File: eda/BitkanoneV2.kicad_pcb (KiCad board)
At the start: 2 copper layers, 140 parts, among them J202 5VUSB, J211 JH23, J212 JL23, J231 Jumper, J232 Jumper, J233 Jumper, J234 Jumper, Q501 PH_NPN, Q502 PH_NPN, U201 BluePill_STM32F103C, U202 MCP2551-I-SN, U301 6DOF, X101 01x02M, X102 01x02M, X200 01x03M, X201 5VUSB, X231 Bus, X232 Bus, X233 Bus, X234 Bus, X401 MotorCon, X42 Conn_01x07_Male, X990 Conn_01x01, X991 Conn_01x01

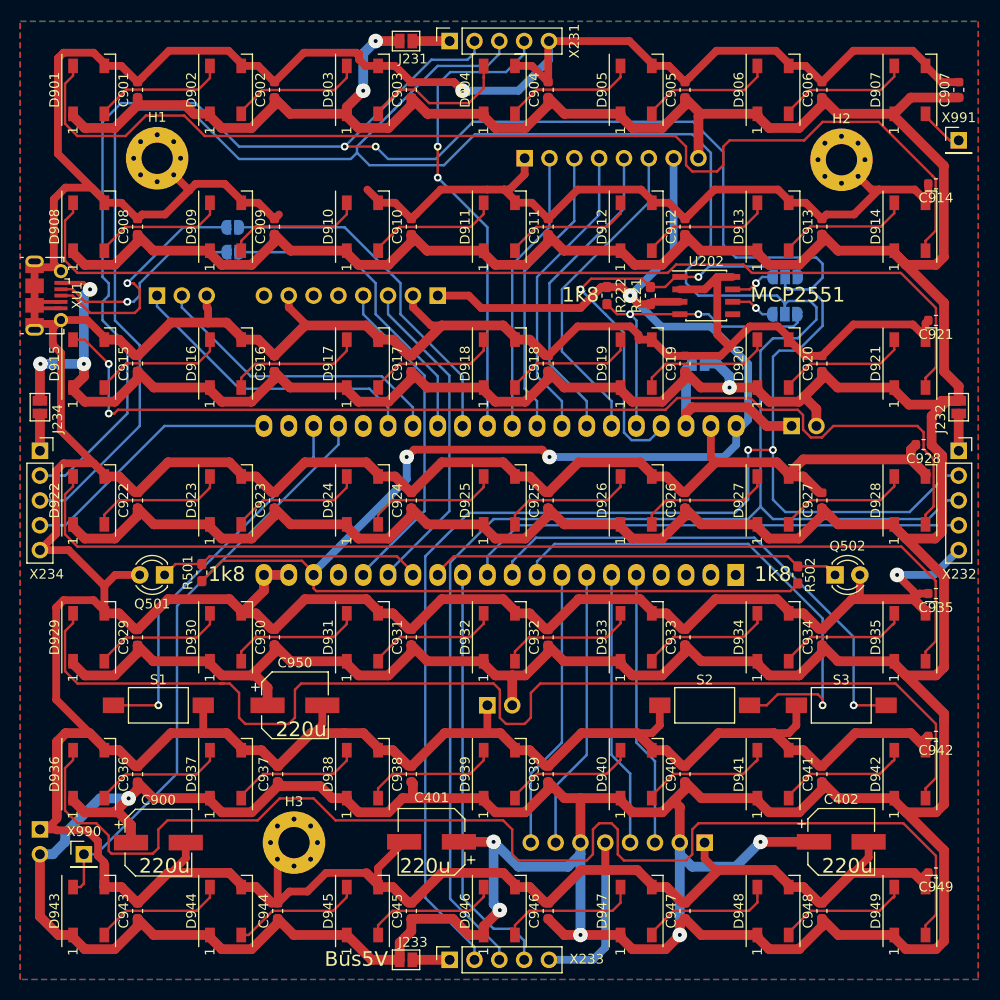
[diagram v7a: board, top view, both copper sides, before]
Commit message: bitkanoneV2 first PCB run ordered
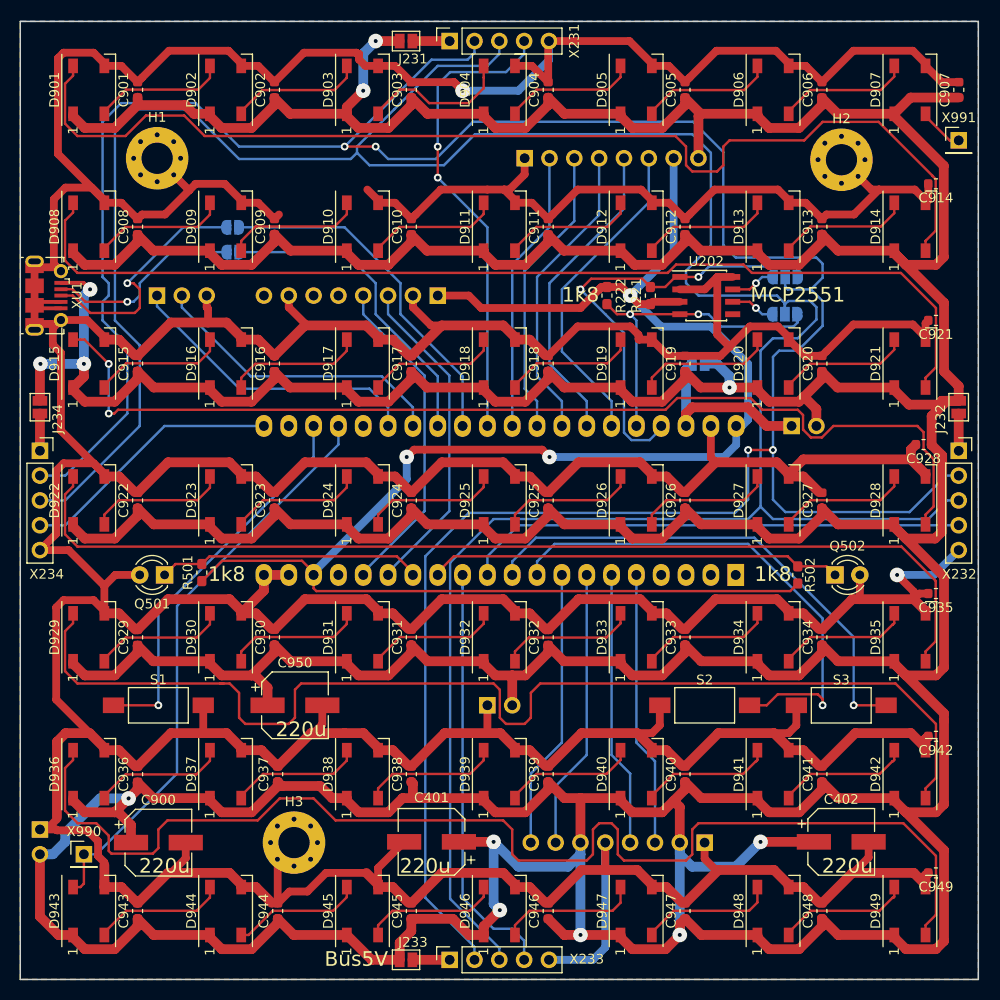
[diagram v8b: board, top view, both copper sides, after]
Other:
- board outline added: 98 x 98 mm
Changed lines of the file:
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@@
   (general
     (thickness 1.6)
-    (drawings 86)
+    (drawings 90)
     (tracks 1602)
     (zones 0)
@@
     (0 F.Cu signal)
     (31 B.Cu signal)
-    (32 B.Adhes user)
-    (33 F.Adhes user)
+    (32 B.Adhes user hide)
+    (33 F.Adhes user hide)
     (34 B.Paste user)
     (35 F.Paste user)
@@
     (38 B.Mask user)
     (39 F.Mask user)
-    (40 Dwgs.User user)
-    (41 Cmts.User user)
-    (42 Eco1.User user)
-    (43 Eco2.User user)
+    (40 Dwgs.User user hide)
+    (41 Cmts.User user hide)
+    (42 Eco1.User user hide)
+    (43 Eco2.User user hide)
     (44 Edge.Cuts user)
-    (45 Margin user)
+    (45 Margin user hide)
     (46 B.CrtYd user hide)
     (47 F.CrtYd user hide)
@@
     (solder_mask_min_width 0.25)
     (aux_axis_origin 0 0)
-    (grid_origin 47.4608 76.62)
+    (grid_origin 20 20)
     (visible_elements FFFFFFFF)
     (pcbplotparams
@@
       (usegerberadvancedattributes false)
       (creategerberjobfile false)
-      (excludeedgelayer true)
-      (linewidth 0.100000)
+      (excludeedgelayer false)
+      (linewidth 0.150000)
       (plotframeref false)
       (viasonmask false)
       (mode 1)
-      (useauxorigin false)
+      (useauxorigin true)
       (hpglpennumber 1)
       (hpglpenspeed 20)
@@
       (plotvalue true)
       (plotinvisibletext false)
-      (padsonsilk false)
+      (padsonsilk true)
       (subtractmaskfromsilk false)
       (outputformat 1)
       (mirror false)
-      (drillshape 1)
+      (drillshape 0)
       (scaleselection 1)
-      (outputdirectory ""))
+      (outputdirectory "plots/"))
   )
   (net 0 "")
@@
     )
   )
+  (gr_line (start 118 20) (end 20 20) (layer Edge.Cuts) (width 0.15))
+  (gr_line (start 118 118) (end 118 20) (layer Edge.Cuts) (width 0.15))
+  (gr_line (start 20 118) (end 118 118) (layer Edge.Cuts) (width 0.15))
+  (gr_line (start 20 20) (end 20 118) (layer Edge.Cuts) (width 0.15))
   (gr_text 98mm (at 103.3408 23.915) (layer B.SilkS)
     (effects (font (size 1.5 1.5) (thickness 0.3)) (justify mirror))
@@
   (segment (start 37.7558 29.45) (end 36.865802 28.560002) (width 1) (layer F.Cu) (net 7))
   (segment (start 24.1883 46.775) (end 24.1583 46.745) (width 0.25) (layer F.Cu) (net 7))
+  (via (at 27.1408 47.41) (size 1.5) (drill 0.4) (layers F.Cu B.Cu) (net 7))
+  (segment (start 24.1583 46.745) (end 26.4758 46.745) (width 0.4) (layer F.Cu) (net 7))
+  (segment (start 26.4758 46.745) (end 27.1408 47.41) (width 0.4) (layer F.Cu) (net 7))
+  (segment (start 26.5058 48.045) (end 27.1408 47.41) (width 1) (layer B.Cu) (net 7))
+  (segment (start 26.5058 55.03) (end 26.5058 48.045) (width 1) (layer B.Cu) (net 7))
   (segment (start 28.6 29.45) (end 28.6 29.2) (width 0.25) (layer F.Cu) (net 8))
   (segment (start 30.82499 26.97501) (end 38.21499 26.97501) (width 0.25) (layer F.Cu) (net 8))
@@
   (segment (start 71.54 115.99) (end 71.54 114.0342) (width 0.25) (layer B.Cu) (net 64))
   (segment (start 71.54 114.0342) (end 70.3208 112.815) (width 0.25) (layer B.Cu) (net 64))
+  (segment (start 22.01 71.54) (end 24.6008 71.54) (width 0.25) (layer B.Cu) (net 65))
+  (segment (start 34.7608 61.38) (end 44.9208 61.38) (width 0.25) (layer B.Cu) (net 65))
+  (segment (start 24.6008 71.54) (end 34.7608 61.38) (width 0.25) (layer B.Cu) (net 65))
   (segment (start 22.01 63.92) (end 22.01 60.11) (width 1) (layer F.Cu) (net 67))
   (segment (start 63.92 115.99) (end 60.11 115.99) (width 1) (layer F.Cu) (net 68))
@@
   (segment (start 53.1758 32.805) (end 42.3808 32.805) (width 0.25) (layer B.Cu) (net 80))
   (segment (start 30.9508 60.11) (end 24.6008 66.46) (width 0.25) (layer B.Cu) (net 80))
+  (segment (start 37.9358 28.36) (end 30.3158 28.36) (width 0.25) (layer B.Cu) (net 80))
+  (segment (start 30.3158 28.36) (end 28.4108 30.265) (width 0.25) (layer B.Cu) (net 80))
+  (segment (start 28.4108 30.265) (end 28.4108 46.14) (width 0.25) (layer B.Cu) (net 80))
+  (segment (start 28.4108 46.14) (end 29.0458 46.775) (width 0.25) (layer B.Cu) (net 80))
+  (segment (start 29.0458 46.775) (end 29.0458 48.045) (width 0.25) (layer B.Cu) (net 80))
+  (segment (start 29.0458 48.045) (end 28.4108 48.68) (width 0.25) (layer B.Cu) (net 80))
+  (segment (start 28.4108 48.68) (end 28.4108 50.585) (width 0.25) (layer B.Cu) (net 80))
+  (segment (start 28.4108 50.585) (end 30.9508 53.125) (width 0.25) (layer B.Cu) (net 80))
   (segment (start 69 23.3308) (end 67.7808 24.55) (width 0.25) (layer B.Cu) (net 81))
   (segment (start 69 22.01) (end 69 23.3308) (width 0.25) (layer B.Cu) (net 81))
@@
   (segment (start 54.4458 33.44) (end 53.8108 34.075) (width 0.25) (layer B.Cu) (net 81))
   (segment (start 42.3808 34.075) (end 37.3008 28.995) (width 0.25) (layer B.Cu) (net 81))
+  (segment (start 37.3008 28.995) (end 31.5858 28.995) (width 0.25) (layer B.Cu) (net 81))
+  (segment (start 29.6808 30.9) (end 29.6808 50.585) (width 0.25) (layer B.Cu) (net 81))
+  (segment (start 31.5858 28.995) (end 29.6808 30.9) (width 0.25) (layer B.Cu) (net 81))
+  (segment (start 29.6808 50.585) (end 32.2208 53.125) (width 0.25) (layer B.Cu) (net 81))
   (segment (start 102.0708 89.955) (end 102.0708 89.955) (width 0.25) (layer B.Cu) (net 84))
   (via (at 102.0708 89.955) (size 0.8) (drill 0.4) (layers F.Cu B.Cu) (net 84))
@@
   (segment (start 36.525 49.247081) (end 43.577919 56.3) (width 0.25) (layer B.Cu) (net 97))
   (segment (start 36.525 48.045) (end 36.525 49.247081) (width 0.25) (layer B.Cu) (net 97))
-  (via (at 27.1408 47.41) (size 1.5) (drill 0.4) (layers F.Cu B.Cu) (net 7))
-  (segment (start 24.1583 46.745) (end 26.4758 46.745) (width 0.4) (layer F.Cu) (net 7))
-  (segment (start 26.4758 46.745) (end 27.1408 47.41) (width 0.4) (layer F.Cu) (net 7))
-  (segment (start 26.5058 48.045) (end 27.1408 47.41) (width 1) (layer B.Cu) (net 7))
-  (segment (start 26.5058 55.03) (end 26.5058 48.045) (width 1) (layer B.Cu) (net 7))
-  (segment (start 22.01 71.54) (end 24.6008 71.54) (width 0.25) (layer B.Cu) (net 65))
-  (segment (start 34.7608 61.38) (end 44.9208 61.38) (width 0.25) (layer B.Cu) (net 65))
-  (segment (start 24.6008 71.54) (end 34.7608 61.38) (width 0.25) (layer B.Cu) (net 65))
-  (segment (start 37.9358 28.36) (end 30.3158 28.36) (width 0.25) (layer B.Cu) (net 80))
-  (segment (start 30.3158 28.36) (end 28.4108 30.265) (width 0.25) (layer B.Cu) (net 80))
-  (segment (start 28.4108 30.265) (end 28.4108 46.14) (width 0.25) (layer B.Cu) (net 80))
-  (segment (start 28.4108 46.14) (end 29.0458 46.775) (width 0.25) (layer B.Cu) (net 80))
-  (segment (start 29.0458 46.775) (end 29.0458 48.045) (width 0.25) (layer B.Cu) (net 80))
-  (segment (start 29.0458 48.045) (end 28.4108 48.68) (width 0.25) (layer B.Cu) (net 80))
-  (segment (start 28.4108 48.68) (end 28.4108 50.585) (width 0.25) (layer B.Cu) (net 80))
-  (segment (start 28.4108 50.585) (end 30.9508 53.125) (width 0.25) (layer B.Cu) (net 80))
-  (segment (start 37.3008 28.995) (end 31.5858 28.995) (width 0.25) (layer B.Cu) (net 81))
-  (segment (start 29.6808 30.9) (end 29.6808 50.585) (width 0.25) (layer B.Cu) (net 81))
-  (segment (start 31.5858 28.995) (end 29.6808 30.9) (width 0.25) (layer B.Cu) (net 81))
-  (segment (start 29.6808 50.585) (end 32.2208 53.125) (width 0.25) (layer B.Cu) (net 81))
   (segment (start 62.7008 56.3) (end 62.7008 61.38) (width 0.25) (layer B.Cu) (net 98))
   (segment (start 56.3508 49.95) (end 62.7008 56.3) (width 0.25) (layer B.Cu) (net 98))
@@
   (segment (start 42.3958 43.6) (end 53.1758 43.6) (width 0.25) (layer B.Cu) (net 98))
   (segment (start 53.1758 43.6) (end 56.3508 46.775) (width 0.25) (layer B.Cu) (net 98))
-  (segment (start 24.1583 47.395) (end 25.356728 47.395) (width 0.25) (layer F.Cu) (net 101))
-  (segment (start 25.356728 47.395) (end 26.641728 48.68) (width 0.25) (layer F.Cu) (net 101))
   (segment (start 53.1758 41.06) (end 42.3808 41.06) (width 0.25) (layer B.Cu) (net 99))
   (segment (start 58.8908 46.775) (end 53.1758 41.06) (width 0.25) (layer B.Cu) (net 99))
@@
   (segment (start 30.9508 46.775) (end 36.6658 41.06) (width 0.25) (layer B.Cu) (net 100))
   (segment (start 36.6658 41.06) (end 41.0808 41.06) (width 0.25) (layer B.Cu) (net 100))
+  (segment (start 24.1583 47.395) (end 25.356728 47.395) (width 0.25) (layer F.Cu) (net 101))
+  (segment (start 25.356728 47.395) (end 26.641728 48.68) (width 0.25) (layer F.Cu) (net 101))
   (segment (start 26.641728 48.68) (end 30.9508 48.68) (width 0.25) (layer F.Cu) (net 101))
   (segment (start 30.9508 48.68) (end 30.9508 48.68) (width 0.25) (layer F.Cu) (net 101))
